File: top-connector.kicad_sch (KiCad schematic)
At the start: 6 parts, among them J1 Plug_Hirose_DF40_2x50_DF40C-1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, Q2 DMG1012T-7

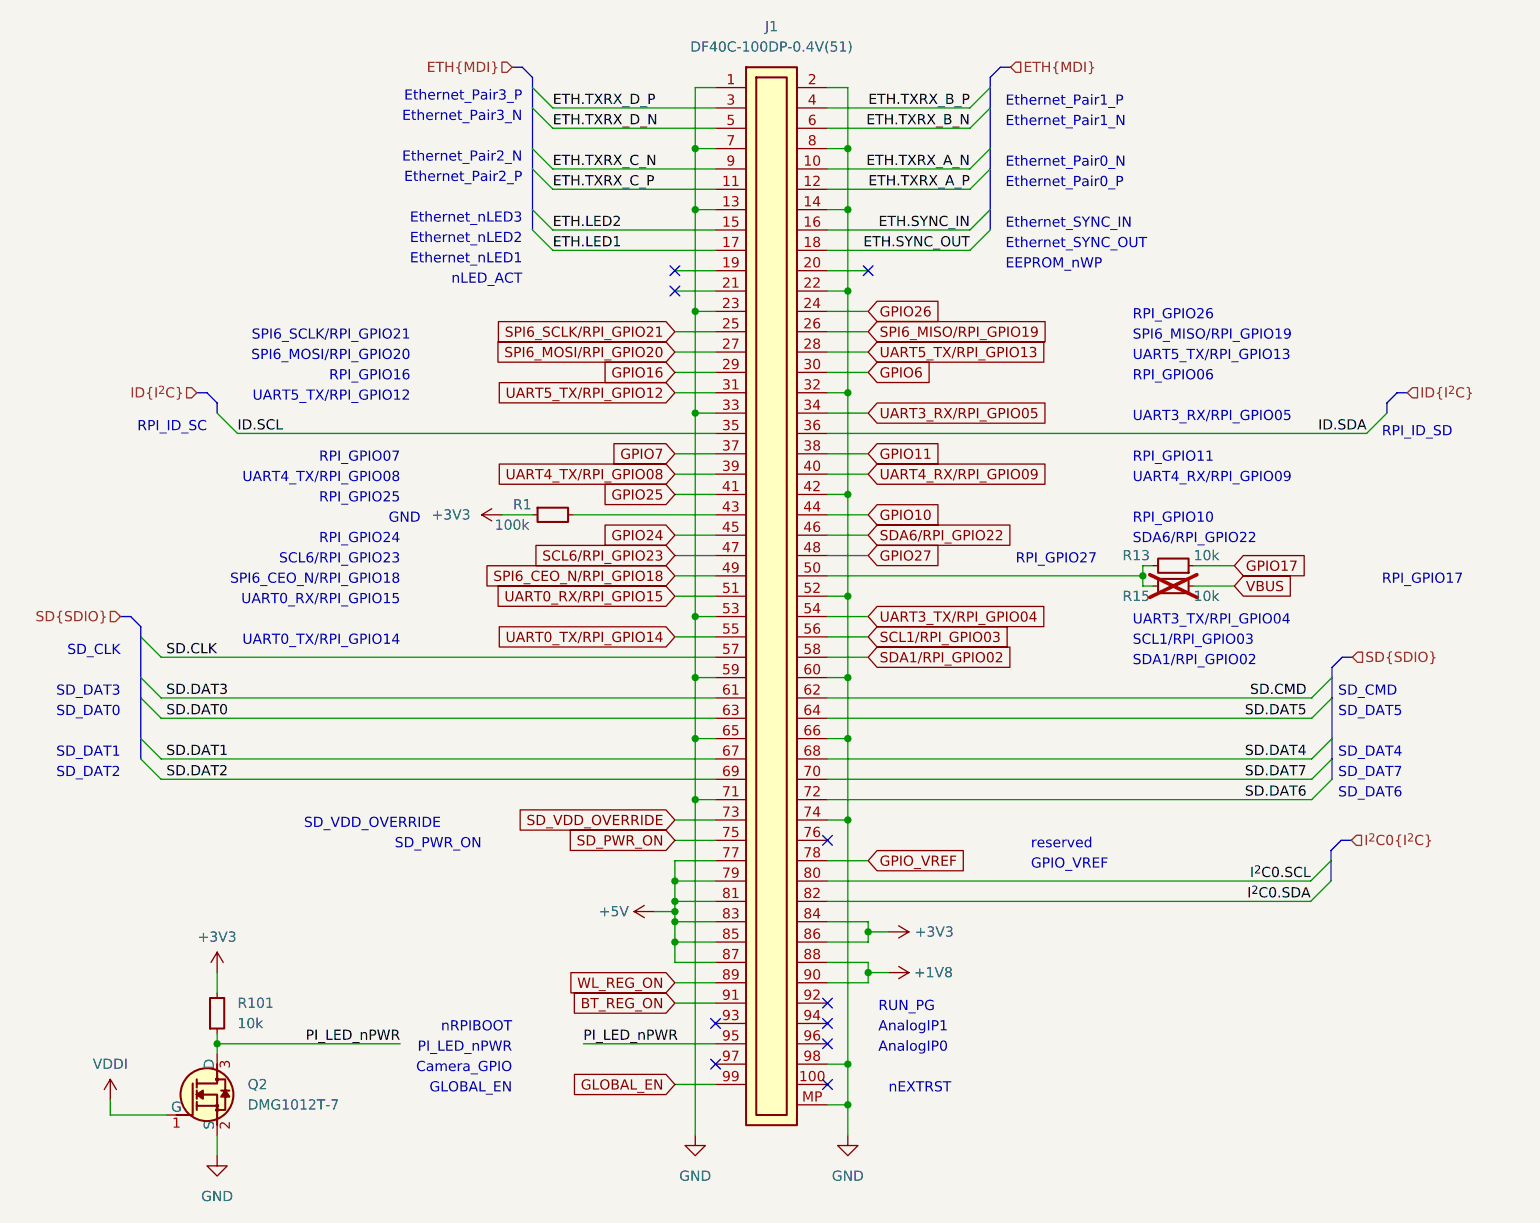
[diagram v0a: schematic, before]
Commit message: [#59910] Align buses, updated symbols and clean ERC
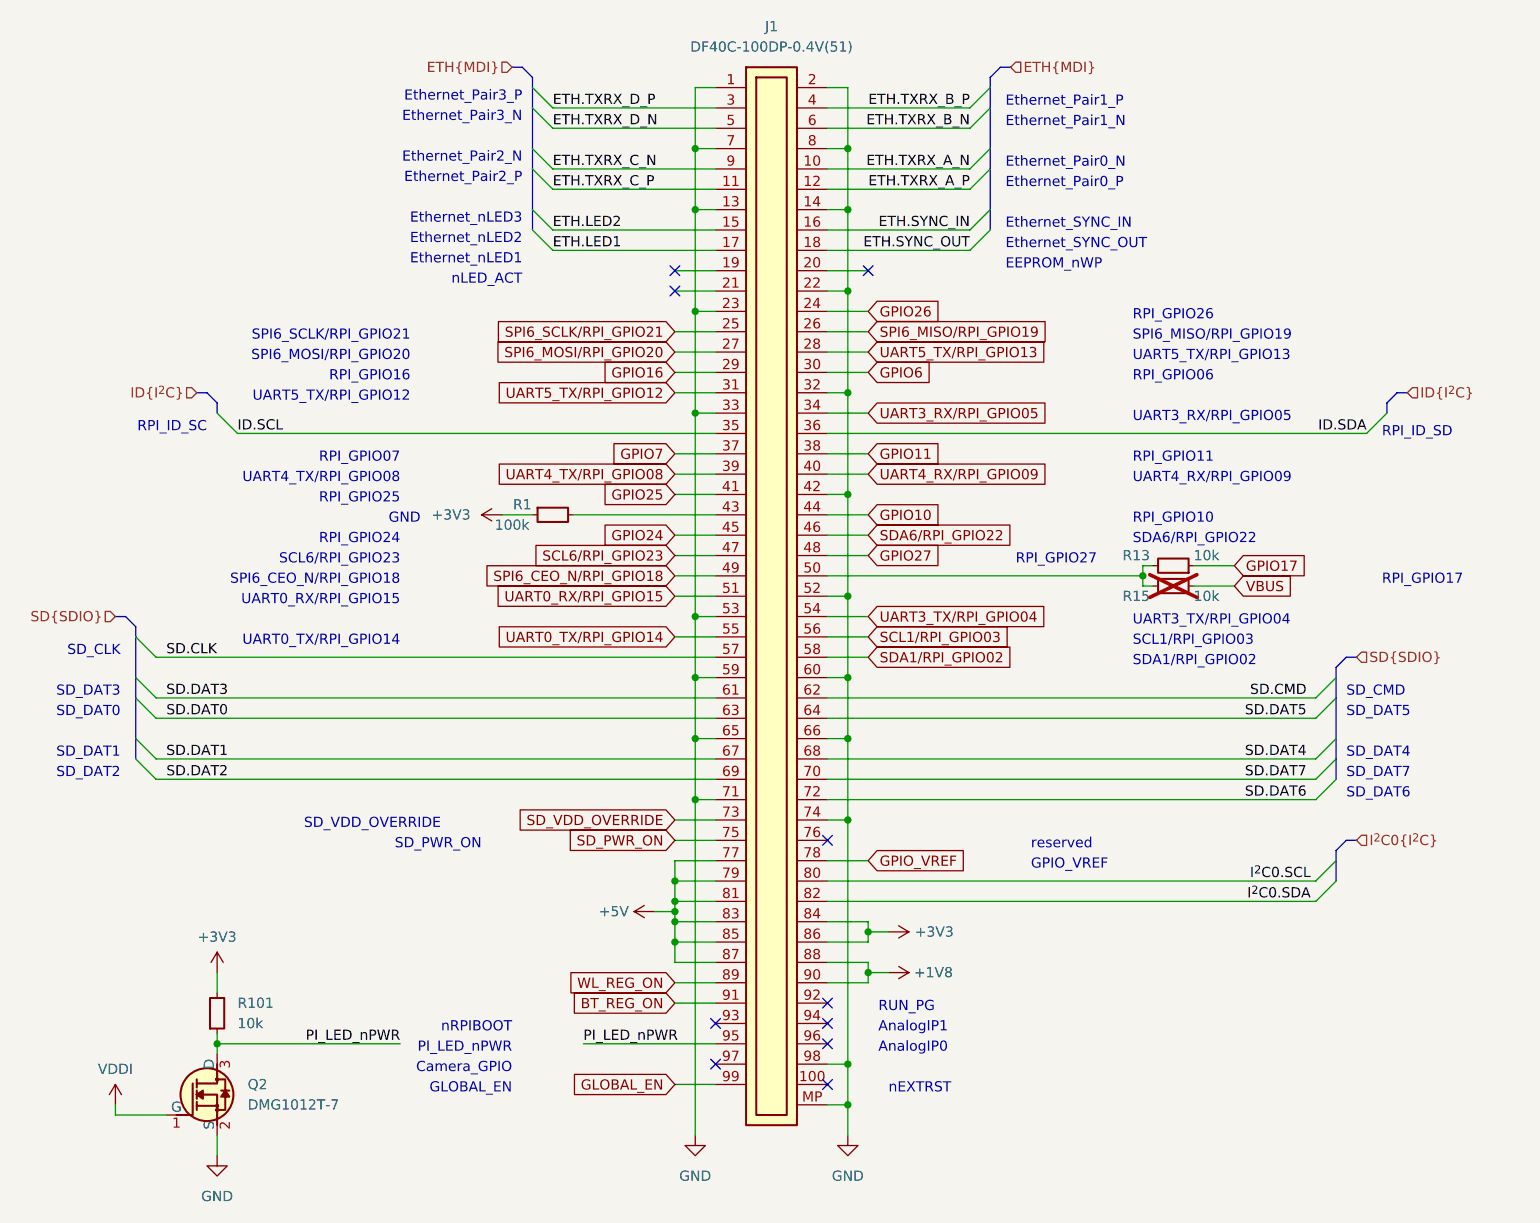
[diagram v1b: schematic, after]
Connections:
- net VDDI renamed VDD

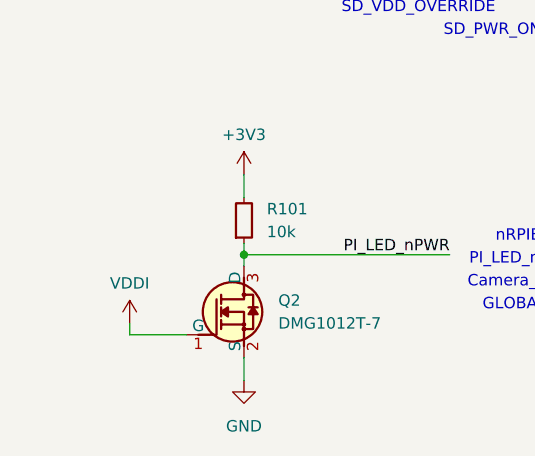
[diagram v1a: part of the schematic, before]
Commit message: [#73079] Migrate project to KiCad 8. Clean DRCs
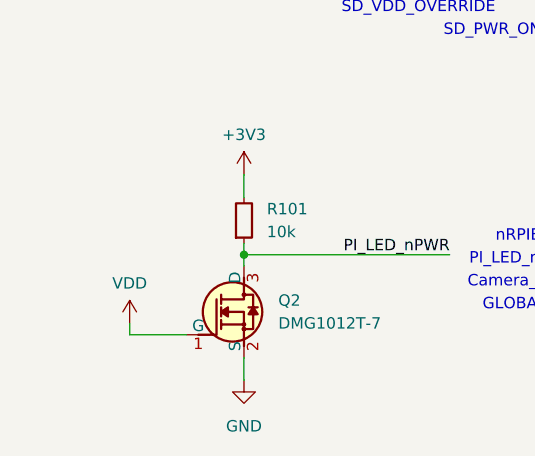
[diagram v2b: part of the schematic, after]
